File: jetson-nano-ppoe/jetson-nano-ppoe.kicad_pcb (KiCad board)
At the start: 2 copper layers, 14 x 79 mm, 32 parts, among them IC1 TPS566238PRQFR, J1 Conn_01x02, J2 Conn_02x05_Odd_Even, J3 Conn_02x02_Odd_Even, Q1 Q_PMOS_GSD, Q2 Q_PMOS_GSD, Q4 Q_NMOS_DUAL

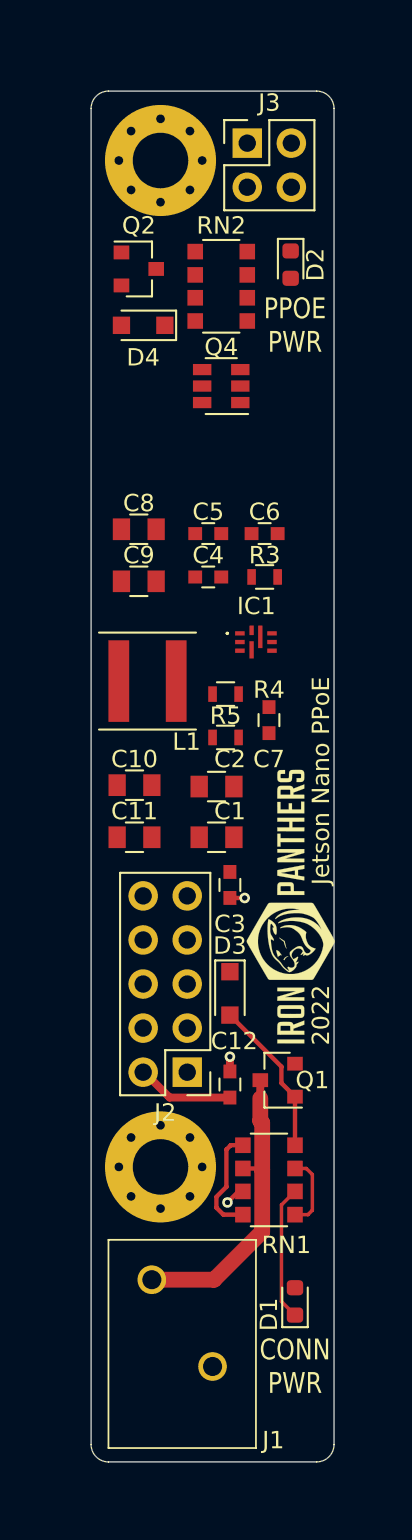
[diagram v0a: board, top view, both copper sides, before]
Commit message: jetson-nano-ppoe more floorplan and spice model attempt
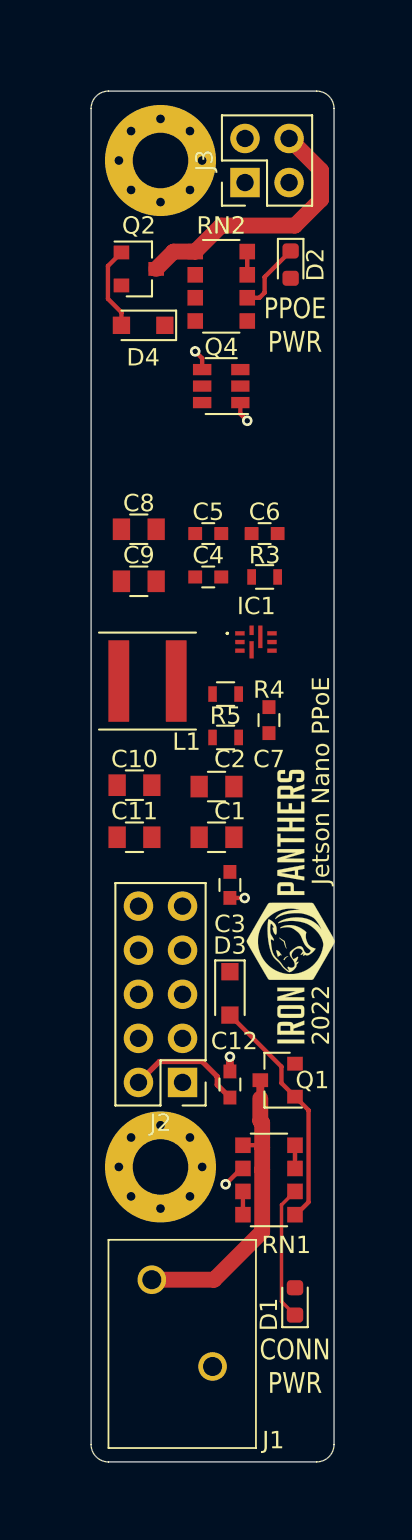
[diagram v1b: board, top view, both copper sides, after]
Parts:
- moved J3 2.27 mm to (154.9, 66.3), turned to 90 degrees
- moved J2 0.65 mm to (151.3, 118.1)
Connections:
- RN1 pad 1: /12V_CONN_R -> /12V_CONN
- RN1 pad 2: /12V_CONN -> GND
- RN1 pad 3: GND -> /12V_G_R
- RN1 pad 4: /12V_CONN_R -> /12V_G_R
- RN1 pad 5: /12V_G_R -> /12V_G
- RN1 pad 7: /12V_G_R -> /12V_CONN_R
- RN1 pad 8: /12V_G -> /12V_CONN_R
- RN2 pad 1: /TR2_TAP_R -> /TR2_TAP
- RN2 pad 2: /TR2_TAP -> GND
- RN2 pad 3: GND -> /12V_2_G_R
- RN2 pad 4: /TR2_TAP_R -> /12V_2_G_R
- RN2 pad 5: /12V_2_G_R -> /12V_2_G
- RN2 pad 7: /12V_2_G_R -> /TR2_TAP_R
- RN2 pad 8: /12V_2_G -> /TR2_TAP_R
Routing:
- net /TR2_TAP: track 0.00 -> 15.4 mm
- net /12V_CONN_R: track 6.34 -> 1.34 mm
- net /12V_2_G: track 0.00 -> 4.85 mm
- net /12V_G: track 9.05 -> 13.7 mm
- net /TR2_TAP_K: track 0.00 -> 4.15 mm
- net /12V_G_R: track 4.31 -> 1.34 mm
- net GND: track 2.86 -> 5.51 mm, vias 3 -> 5
- net /TR2_TAP_R: track 0.00 -> 1.34 mm
- net +5V: track 5.60 -> 6.91 mm

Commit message: jetson-nano-ppoe layout r1
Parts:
- added G***: LOGO, frc-on-ftc-hw:iron_panthers_logo_fcu_5mm, B.Cu at (148.8, 137.5)
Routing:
- net /12V_G_R: track 1.34 -> 86.0 mm, vias 0 -> 2
- net /12V_CONN_R: track 1.34 -> 48.0 mm, vias 0 -> 2
- net GND: track 5.51 -> 30.3 mm, vias 5 -> 24
- net +5V: track 6.91 -> 24.3 mm
- net /12V_2_G: track 4.85 -> 18.8 mm, vias 0 -> 2
- net /IC1_FB: track 0.00 -> 13.6 mm, vias 0 -> 2
- net +12V: track 0.00 -> 11.9 mm
- net /TR2_TAP_R: track 1.34 -> 10.7 mm, vias 0 -> 2
- net /IC1_SW: track 0.00 -> 7.66 mm
- net /IC1_SS: track 0.00 -> 6.30 mm
- net /12V_2_G_R: track 0.00 -> 5.22 mm
- net /IC1_BST: track 0.00 -> 4.78 mm
- net /IC1_VCC: track 0.00 -> 4.18 mm
- net /IC1_BST_R: track 0.00 -> 2.50 mm
- net /12V_CONN_K: track 7.77 -> 9.32 mm
- added copper zone on F.Cu, net +12V
- added copper zone on F.Cu, net +5V
- added copper zone on F.Cu, net /IC1_SW
- added copper zone on B.Cu, net GND
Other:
- board text added: "Iron Panthers"
- board text added: "Jetson Nano PPoE R1 2022"
- board text added: "ihartwig@"
- board text removed: "2022"
